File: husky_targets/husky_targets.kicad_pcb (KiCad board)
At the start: 2 copper layers, 34.3 x 8.4 mm, 3 parts, among them J1 HUSKEY_EDGE_CONNECTOR, J2 USB_C_Receptacle, U1 RP2350_60QFN

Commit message: finishing the schematic, starting with the layout
Signed-off-by: nitrogar <kernel101@yandex.com>
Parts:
- added C1: 100n, Capacitor_SMD:C_0603_1608Metric_Pad1.08x0.95mm_HandSolder, F.Cu at (48.9, 136.4)
- added C10: 2u2, Capacitor_SMD:C_0603_1608Metric_Pad1.08x0.95mm_HandSolder, F.Cu at (53.2, 138.9)
- added C13: 100n, Capacitor_SMD:C_0603_1608Metric_Pad1.08x0.95mm_HandSolder, F.Cu at (53.2, 141.4)
- added C14: 100n, Capacitor_SMD:C_0603_1608Metric_Pad1.08x0.95mm_HandSolder, F.Cu at (53.2, 144.0)
- added C15: 100n, Capacitor_SMD:C_0603_1608Metric_Pad1.08x0.95mm_HandSolder, F.Cu at (53.2, 146.5)
- added C16: 100n, Capacitor_SMD:C_0603_1608Metric_Pad1.08x0.95mm_HandSolder, F.Cu at (53.2, 149.0)
- added C19: 100n, Capacitor_SMD:C_0603_1608Metric_Pad1.08x0.95mm_HandSolder, F.Cu at (53.2, 151.5)
- added C2: 100n, Capacitor_SMD:C_0603_1608Metric_Pad1.08x0.95mm_HandSolder, F.Cu at (48.9, 138.9)
- added C20: 100n, Capacitor_SMD:C_0603_1608Metric_Pad1.08x0.95mm_HandSolder, F.Cu at (53.2, 154.0)
- added C21: 100n, Capacitor_SMD:C_0603_1608Metric_Pad1.08x0.95mm_HandSolder, F.Cu at (57.6, 136.4)
- added C3: 100n, Capacitor_SMD:C_0603_1608Metric_Pad1.08x0.95mm_HandSolder, F.Cu at (48.9, 141.4)
- added C4: 100n, Capacitor_SMD:C_0603_1608Metric_Pad1.08x0.95mm_HandSolder, F.Cu at (48.9, 144.0)
- added C5: 100n, Capacitor_SMD:C_0603_1608Metric_Pad1.08x0.95mm_HandSolder, F.Cu at (48.9, 146.5)
- added C6: 100n, Capacitor_SMD:C_0603_1608Metric_Pad1.08x0.95mm_HandSolder, F.Cu at (48.9, 149.0)
- added C7: 100n, Capacitor_SMD:C_0603_1608Metric_Pad1.08x0.95mm_HandSolder, F.Cu at (48.9, 151.5)
- added C8: 100n, Capacitor_SMD:C_0603_1608Metric_Pad1.08x0.95mm_HandSolder, F.Cu at (48.9, 154.0)
- added C9: 100n, Capacitor_SMD:C_0603_1608Metric_Pad1.08x0.95mm_HandSolder, F.Cu at (53.2, 136.4)
- added J10: Conn_01x01, Connector_PinHeader_1.27mm:PinHeader_1x01_P1.27mm_Vertical, F.Cu at (257.8, 134.0)
- added J11: Conn_01x01, Connector_PinHeader_1.27mm:PinHeader_1x01_P1.27mm_Vertical, F.Cu at (257.8, 137.3)
- added J12: Conn_01x01, Connector_PinHeader_1.27mm:PinHeader_1x01_P1.27mm_Vertical, F.Cu at (257.8, 140.7)
- added J3: Conn_01x04_Pin, Connector_PinHeader_2.54mm:PinHeader_1x04_P2.54mm_Vertical, F.Cu at (262.2, 134.6)
- added J4: Conn_01x02_Pin, Connector_PinHeader_1.27mm:PinHeader_1x02_P1.27mm_Vertical, F.Cu at (266.6, 140.8)
- added J5: Conn_01x01, Connector_PinHeader_1.27mm:PinHeader_1x01_P1.27mm_Vertical, F.Cu at (253.6, 134.0)
- added J6: Conn_01x01, Connector_PinHeader_1.27mm:PinHeader_1x01_P1.27mm_Vertical, F.Cu at (253.6, 137.3)
- added J7: Conn_01x01, Connector_PinHeader_1.27mm:PinHeader_1x01_P1.27mm_Vertical, F.Cu at (253.6, 140.7)
- added J8: Conn_01x01, Connector_PinHeader_1.27mm:PinHeader_1x01_P1.27mm_Vertical, F.Cu at (253.6, 144.0)
- added J9: Conn_01x01, Connector_PinHeader_1.27mm:PinHeader_1x01_P1.27mm_Vertical, F.Cu at (253.6, 147.4)
- added R1: 5.11k, Resistor_SMD:R_0603_1608Metric_Pad0.98x0.95mm_HandSolder, F.Cu at (57.6, 138.9)
- added R10: 10, Resistor_SMD:R_0603_1608Metric_Pad0.98x0.95mm_HandSolder, F.Cu at (61.9, 141.4)
- added R11: 3k3, Resistor_SMD:R_0603_1608Metric_Pad0.98x0.95mm_HandSolder, F.Cu at (61.9, 144.0)
- added R12: 5k6, Resistor_SMD:R_0603_1608Metric_Pad0.98x0.95mm_HandSolder, F.Cu at (61.9, 146.5)
- added R2: 5.11k, Resistor_SMD:R_0603_1608Metric_Pad0.98x0.95mm_HandSolder, F.Cu at (57.6, 141.4)
- added R3: 1M, Resistor_SMD:R_0603_1608Metric_Pad0.98x0.95mm_HandSolder, F.Cu at (57.6, 144.0)
- added R4: 10, Resistor_SMD:R_0603_1608Metric_Pad0.98x0.95mm_HandSolder, F.Cu at (57.6, 146.5)
- added R5: DNF, Resistor_SMD:R_0603_1608Metric_Pad0.98x0.95mm_HandSolder, F.Cu at (57.6, 149.0)
- added R6: 0, Resistor_SMD:R_0603_1608Metric_Pad0.98x0.95mm_HandSolder, F.Cu at (57.6, 151.5)
- added R7: 1k, Resistor_SMD:R_0603_1608Metric_Pad0.98x0.95mm_HandSolder, F.Cu at (57.6, 154.0)
- added R8: 27, Resistor_SMD:R_0603_1608Metric_Pad0.98x0.95mm_HandSolder, F.Cu at (149.2, 118.8)
- added R9: 27, Resistor_SMD:R_0603_1608Metric_Pad0.98x0.95mm_HandSolder, F.Cu at (149.2, 117.2)
- added U2: W25Q128JVS, Package_SO:SOIC-8_5.3x5.3mm_P1.27mm, F.Cu at (152.8, 106.5)
- J2: value USB_C_Receptacle -> USB_C_Receptacle_USB2.0_16P; footprint Connector_USB:USB_C_Receptacle_Amphenol_12401548E4-2A -> Connector_USB:USB_C_Receptacle_G-Switch_GT-USB-7010ASV
- moved J2 21.1 mm to (132.7, 119.4), turned to 90 degrees
- moved U1 6.52 mm to (156.2, 118.8), turned to 90 degrees
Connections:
- net Net-(J2-VBUS-PadA4) renamed +5V
- J1 pad A3: FILT_LP -> FILT_HP
- J1 pad A5: VCC3.3 -> ADC_VDD
- J1 pad B1: SHUNTL -> ADC_VDD
- J1 pad B2: SHUNTH -> FILT_HP
- J1 pad B5: FILTIN -> DVDD
- J1 pad B6: VCC1.0 -> DVDD
- J2 pad A1: Net-(J2-GND-PadA1) -> GND
- J2 pad A12: Net-(J2-GND-PadA1) -> GND
- J2 pad A5: unconnected-(J2-CC1-PadA5) -> Net-(J2-CC1)
- J2 pad A6: unconnected-(J2-D+-PadA6) -> D+
- J2 pad A7: unconnected-(J2-D--PadA7) -> D-
- J2 pad B1: Net-(J2-GND-PadA1) -> GND
- J2 pad B12: Net-(J2-GND-PadA1) -> GND
- J2 pad B5: unconnected-(J2-CC2-PadB5) -> Net-(J2-CC2)
- J2 pad B6: unconnected-(J2-D+-PadB6) -> D+
- J2 pad B7: unconnected-(J2-D--PadB7) -> D-
- J2 pad S1: unconnected-(J2-SHIELD-PadS1) -> Net-(J2-SHIELD)
- U1 pad 1: unconnected-(U1-IOVDD-Pad1) -> ADC_VDD
- U1 pad 11: unconnected-(U1-IOVDD-Pad11) -> ADC_VDD
- U1 pad 2: unconnected-(U1-GPIO0-Pad2) -> GPIO1/TX
- U1 pad 20: unconnected-(U1-IOVDD-Pad20) -> ADC_VDD
- U1 pad 21: unconnected-(U1-XIN-Pad21) -> Net-(U1-XIN)
- U1 pad 23: unconnected-(U1-DVDD-Pad23) -> DVDD
- U1 pad 24: unconnected-(U1-SWCLK-Pad24) -> SWCLK
- U1 pad 25: unconnected-(U1-SWD-Pad25) -> SWD
- U1 pad 26: unconnected-(U1-RUN-Pad26) -> nRST
- U1 pad 3: unconnected-(U1-GPIO1-Pad3) -> GPIO2/RX
- U1 pad 30: unconnected-(U1-IOVDD-Pad30) -> ADC_VDD
- U1 pad 35: unconnected-(U1-GPIO23-Pad35) -> LED1
- U1 pad 36: unconnected-(U1-GPIO24-Pad36) -> LED2
- U1 pad 37: unconnected-(U1-GPIO25-Pad37) -> LED3
- U1 pad 38: unconnected-(U1-IOVDD-Pad38) -> ADC_VDD
- U1 pad 39: unconnected-(U1-DVDD-Pad39) -> DVDD
- U1 pad 4: unconnected-(U1-GPIO2-Pad4) -> GPIO3
- U1 pad 44: unconnected-(U1-ADC_AVDD-Pad44) -> ADC_VDD
- U1 pad 45: unconnected-(U1-IOVDD-Pad45) -> ADC_VDD
- U1 pad 46: unconnected-(U1-VREG_AVDD-Pad46) -> ADC_VDD
- U1 pad 47: unconnected-(U1-VREG_PGND-Pad47) -> GND
- U1 pad 49: unconnected-(U1-VREG_VIN-Pad49) -> ADC_VDD
- U1 pad 5: unconnected-(U1-GPIO3-Pad5) -> GPIO4
- U1 pad 50: unconnected-(U1-VREG_FB-Pad50) -> Net-(U1-VREG_FB)
- U1 pad 51: unconnected-(U1-USB_DM-Pad51) -> DN
- U1 pad 52: unconnected-(U1-USB_DP-Pad52) -> DP
- U1 pad 53: unconnected-(U1-USB_OTP_VDD-Pad53) -> ADC_VDD
- U1 pad 54: unconnected-(U1-QSPI_IOVDD-Pad54) -> ADC_VDD
- U1 pad 55: unconnected-(U1-QSPI_SD3-Pad55) -> QSPI_SD3
- U1 pad 56: unconnected-(U1-QSPI_SCLK-Pad56) -> QSPI_SCLK
- U1 pad 57: unconnected-(U1-QSPI_SD0-Pad57) -> QSPI_SD0
- U1 pad 58: unconnected-(U1-QSPI_SD2-Pad58) -> QSPI_SD2
- U1 pad 59: unconnected-(U1-QSPI_SD1-Pad59) -> QSPI_SD1
- U1 pad 6: unconnected-(U1-DVDD-Pad6) -> DVDD
- U1 pad 60: unconnected-(U1-QSPI_SS-Pad60) -> QSPI_SS
- U1 pad 61: unconnected-(U1-GND-Pad61) -> GND
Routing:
- net D-: track 0.00 -> 20.1 mm
- net D+: track 0.00 -> 19.7 mm
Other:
- board size 34.3 x 8.4 mm -> 50.3 x 42.1 mm
- copper layers 2 -> 4

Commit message: done most of the pcb layout except the usb differntial pairs, well look for it later
Signed-off-by: nitrogar <kernel101@yandex.com>
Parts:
- removed R3: 1M, Resistor_SMD:R_0603_1608Metric_Pad0.98x0.95mm_HandSolder
- moved C6 118.8 mm to (161.8, 111.8)
- moved R7 117.0 mm to (172.0, 129.8)
- moved C9 116.6 mm to (168.0, 116.0), turned to 180 degrees
- moved C3 115.7 mm to (161.8, 116.0)
- moved R6 113.5 mm to (168.8, 128.6), turned to 90 degrees
- moved C7 113.1 mm to (157.5, 120.0), turned to -90 degrees
- moved C8 112.6 mm to (157.2, 123.2)
- moved R5 112.5 mm to (166.8, 121.8), turned to -90 degrees
- moved C13 112.1 mm to (161.8, 113.5)
- moved C1 111.9 mm to (156.8, 106.5), turned to 90 degrees
- moved C20 111.3 mm to (159.2, 120.0), turned to -90 degrees
- moved C15 109.3 mm to (155.0, 106.5), turned to 90 degrees
- moved C2 108.6 mm to (152.5, 106.5), turned to 90 degrees
- moved R4 107.0 mm to (155.0, 102.2), turned to -90 degrees
- moved C4 104.7 mm to (149.0, 113.2), turned to 180 degrees
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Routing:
- net ADC_VDD: track 0.00 -> 51.2 mm
- net LED1: track 0.00 -> 27.8 mm, vias 0 -> 2
- net LED3: track 0.00 -> 27.2 mm, vias 0 -> 2
- net LED2: track 0.00 -> 27.0 mm, vias 0 -> 4
- net QSPI_SD0: track 0.00 -> 25.9 mm, vias 0 -> 6
- net GND: track 0.00 -> 25.5 mm, vias 0 -> 17
- net QSPI_SS: track 0.00 -> 23.3 mm, vias 0 -> 8
- net QSPI_SD2: track 0.00 -> 19.2 mm, vias 0 -> 2
- net QSPI_SCLK: track 0.00 -> 18.8 mm, vias 0 -> 4
- net QSPI_SD3: track 0.00 -> 18.4 mm, vias 0 -> 2
- net QSPI_SD1: track 0.00 -> 17.8 mm, vias 0 -> 2
- net DVDD: track 0.00 -> 16.2 mm, vias 0 -> 6
- net D+: track 19.7 -> 31.1 mm, vias 0 -> 2
- net D-: track 20.1 -> 30.3 mm, vias 0 -> 2
- net Net-(U1-VREG_FB): track 0.00 -> 9.59 mm
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- added copper zone on F.Cu, net ADC_VDD
- added copper zone on In2.Cu, net DVDD
- added copper zone on B.Cu, net GND
- added copper zone on In1.Cu, net GND

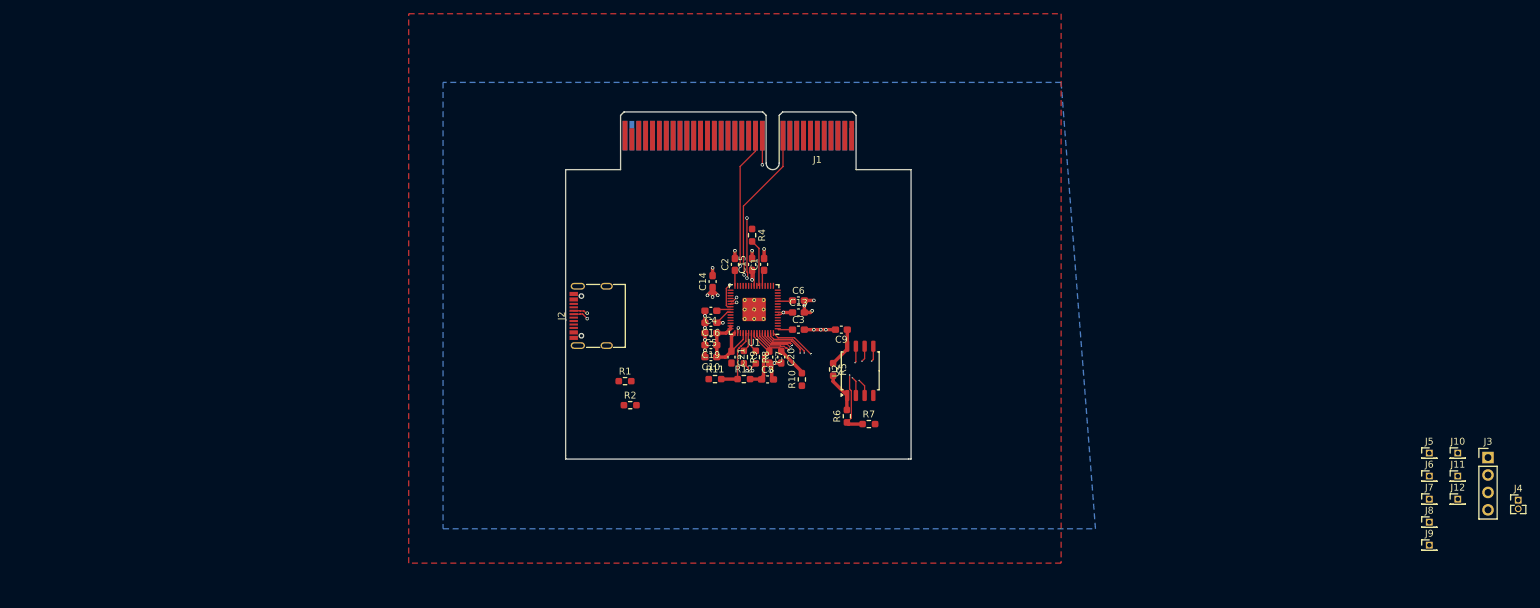
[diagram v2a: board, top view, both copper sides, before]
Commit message: done first version of RP2350 OTPVDD board
Signed-off-by: nitrogar <kernel101@yandex.com>
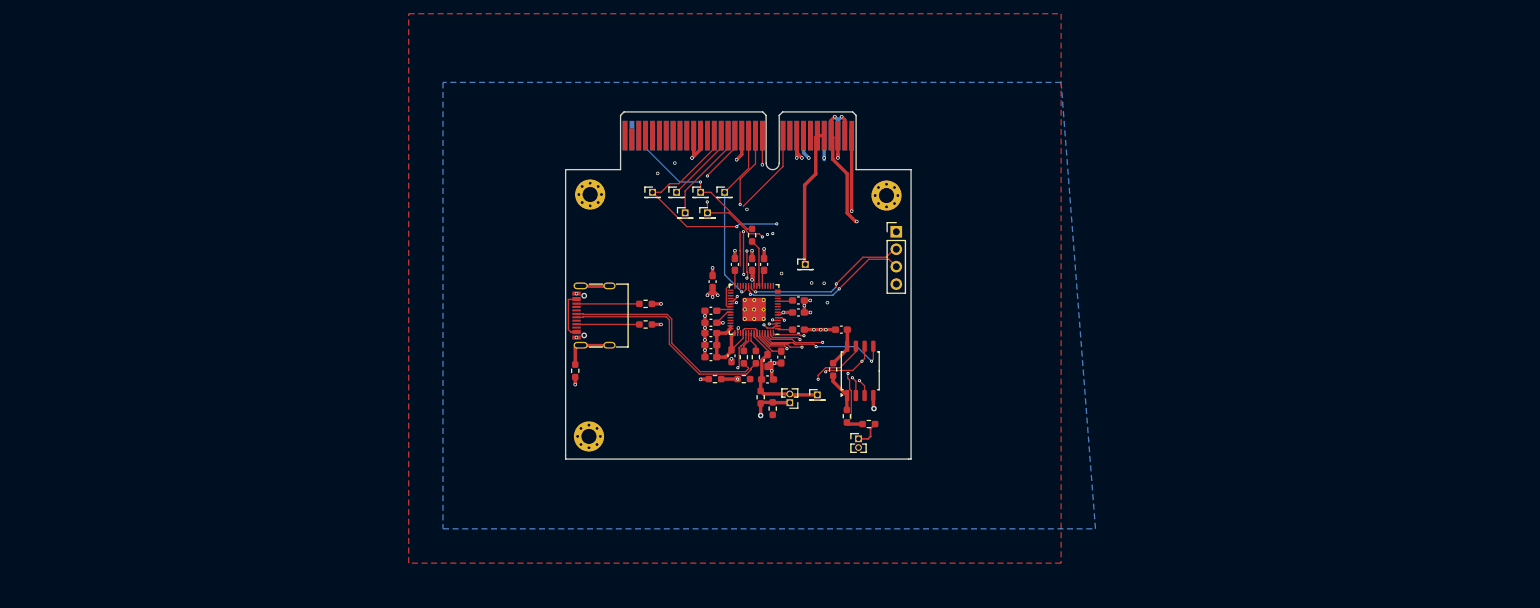
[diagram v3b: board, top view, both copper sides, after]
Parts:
- added H1: MountingHole_Pad_MP, MountingHole:MountingHole_2.2mm_M2_Pad_Via, F.Cu at (174.6, 96.5)
- added H2: MountingHole_Pad_MP, MountingHole:MountingHole_2.2mm_M2_Pad_Via, F.Cu at (131.2, 131.6)
- added H3: MountingHole_Pad_MP, MountingHole:MountingHole_2.2mm_M2_Pad_Via, F.Cu at (131.4, 96.3)
- added J13: Conn_01x02_Pin, Connector_PinHeader_1.27mm:PinHeader_1x02_P1.27mm_Vertical, F.Cu at (160.5, 126.6)
- added R13: 0, Resistor_SMD:R_0603_1608Metric_Pad0.98x0.95mm_HandSolder, F.Cu at (158.0, 127.5)
- added R3: 1M, Resistor_SMD:R_0603_1608Metric_Pad0.98x0.95mm_HandSolder, F.Cu at (129.2, 122.0)
- C14: value 100n -> 2u2
- moved J9 124.2 mm to (140.5, 96.0)
- moved J10 119.9 mm to (144.0, 96.0)
- moved J11 118.9 mm to (145.2, 99.0)
- moved J12 116.9 mm to (148.5, 99.0)
- moved J7 115.1 mm to (147.5, 96.0)
- moved J8 113.3 mm to (151.0, 96.0)
- moved J4 96.5 mm to (170.5, 131.9)
- moved J6 95.9 mm to (162.8, 106.5)
- moved J3 92.2 mm to (176.0, 101.8)
- moved J5 89.5 mm to (164.5, 125.5)
- moved R2 12.0 mm to (139.5, 115.2)
- moved R1 11.6 mm to (139.5, 112.2)
- moved R10 6.53 mm to (156.2, 125.8)
- moved C7 0.56 mm to (157.2, 120.5)
- moved J2 0.41 mm to (133.2, 114.0)
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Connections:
- C7 pad 1: ADC_VDD -> SHUNTL
- C8 pad 1: ADC_VDD -> SHUNTL
- J1 pad B1: ADC_VDD -> SHUNTL
- J3 pad 2: SWD -> SWCLK
- J3 pad 3: SWCLK -> SWD
- J5 pad 1: ADC_VDD -> SHUNTL
- R10 pad 1: ADC_VDD -> FILT_HP
- R10 pad 2: ADC_VDD -> SHUNTL
- U1 pad 53: ADC_VDD -> SHUNTL
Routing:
- net FILT_HP: track 0.00 -> 62.6 mm, vias 0 -> 4
- net SHUNTL: track 0.00 -> 59.8 mm, vias 0 -> 1
- net GPIO4: track 0.00 -> 49.4 mm, vias 0 -> 3
- net GPIO2/RX: track 0.00 -> 41.6 mm, vias 0 -> 2
- net GND: track 25.5 -> 66.9 mm, vias 17 -> 46
- net GPIO3: track 0.00 -> 41.1 mm, vias 0 -> 2
- net GPIO1/TX: track 0.00 -> 38.2 mm, vias 0 -> 4
- net nRST: track 0.00 -> 26.5 mm, vias 0 -> 1
- net SWD: track 0.00 -> 25.7 mm, vias 0 -> 2
- net SWCLK: track 0.00 -> 24.9 mm, vias 0 -> 2
- net CLIKIN: track 0.00 -> 23.1 mm, vias 0 -> 1
- net Net-(J2-SHIELD): track 0.00 -> 21.9 mm
- net DVDD: track 16.2 -> 36.8 mm
- net Net-(J2-CC2): track 0.00 -> 9.56 mm
- net Net-(J2-CC1): track 0.00 -> 9.56 mm
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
